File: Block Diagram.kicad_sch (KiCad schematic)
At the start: 0 parts

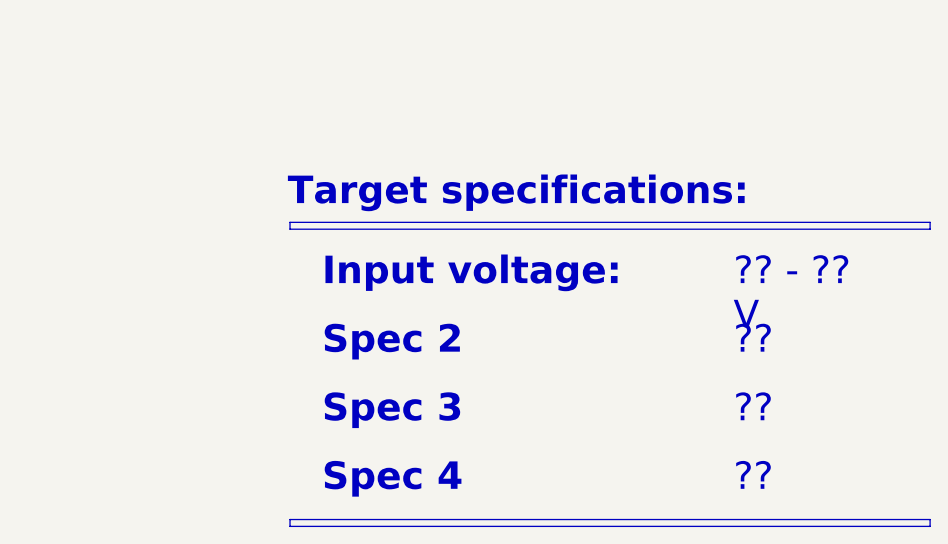
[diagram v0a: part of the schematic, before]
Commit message: Changed resistor position
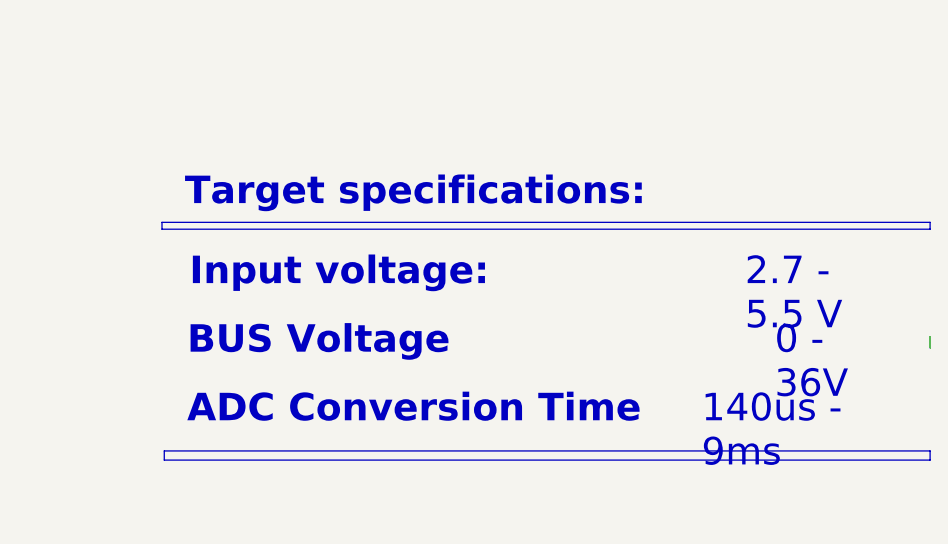
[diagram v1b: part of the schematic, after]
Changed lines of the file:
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@@
 	)
 	(rectangle
-		(start 331.47 237.49)
-		(end 402.59 238.252)
+		(start 317.5 229.87)
+		(end 402.59 230.886)
 		(stroke
 			(width 0)
@@
 	)
 	(rectangle
-		(start 331.47 204.47)
+		(start 317.246 204.47)
 		(end 402.59 205.232)
 		(stroke
@@
 		)
 	)
-	(text_box "Spec 3"
-		(exclude_from_sim no)
-		(at 332.74 220.98 0)
-		(size 41.91 7.62)
+	(text_box "ADC Conversion Time"
+		(exclude_from_sim no)
+		(at 317.754 220.98 0)
+		(size 56.896 7.62)
 		(margins 2.2859 2.2859 2.2859 2.2859)
 		(stroke
 			(width -0.0001)
-			(type default)
+			(type solid)
 		)
 		(fill
@@
 		)
 	)
-	(text_box "Spec 2"
-		(exclude_from_sim no)
-		(at 332.74 213.36 0)
+	(text_box "BUS Voltage"
+		(exclude_from_sim no)
+		(at 317.754 213.36 0)
 		(size 43.18 7.62)
 		(margins 2.2859 2.2859 2.2859 2.2859)
 		(stroke
 			(width -0.0001)
-			(type default)
+			(type solid)
 		)
 		(fill
@@
 	(text_box "Input voltage:"
 		(exclude_from_sim no)
-		(at 332.74 205.74 0)
+		(at 318.008 205.74 0)
 		(size 41.91 7.62)
 		(margins 2.2859 2.2859 2.2859 2.2859)
@@
 		)
 	)
-	(text_box "??"
-		(exclude_from_sim no)
-		(at 378.46 228.6 0)
+	(text_box "0 - 36V"
+		(exclude_from_sim no)
+		(at 383.032 213.36 0)
 		(size 24.13 7.62)
 		(margins 2.2859 2.2859 2.2859 2.2859)
 		(stroke
 			(width -0.0001)
-			(type default)
-		)
-		(fill
-			(type none)
-		)
-		(effects
-			(font
-				(face "Times New Roman")
-				(size 3.048 3.048)
-				(color 0 0 0 1)
-			)
-			(justify left top)
-		)
-	)
-	(text_box "??"
-		(exclude_from_sim no)
-		(at 378.46 213.36 0)
-		(size 24.13 7.62)
-		(margins 2.2859 2.2859 2.2859 2.2859)
-		(stroke
-			(width -0.0001)
-			(type default)
+			(type solid)
 		)
 		(fill
@@
 	(text_box "Target specifications:"
 		(exclude_from_sim no)
-		(at 328.93 196.85 0)
-		(size 73.66 7.62)
+		(at 317.5 196.85 0)
+		(size 85.09 7.62)
 		(margins 2.2859 2.2859 2.2859 2.2859)
 		(stroke
@@
 		)
 	)
-	(text_box "??"
-		(exclude_from_sim no)
-		(at 378.46 220.98 0)
-		(size 24.13 7.62)
+	(text_box "140us - 9ms"
+		(exclude_from_sim no)
+		(at 374.904 220.98 0)
+		(size 27.686 7.62)
 		(margins 2.2859 2.2859 2.2859 2.2859)
 		(stroke
 			(width -0.0001)
-			(type default)
+			(type solid)
 		)
 		(fill
@@
 		)
 	)
-	(text_box "?? - ?? V"
-		(exclude_from_sim no)
-		(at 378.46 205.74 0)
+	(text_box "2.7 - 5.5 V"
+		(exclude_from_sim no)
+		(at 379.73 205.74 0)
 		(size 24.13 7.62)
 		(margins 2.2859 2.2859 2.2859 2.2859)
 		(stroke
 			(width -0.0001)
-			(type default)
+			(type solid)
 		)
 		(fill
@@
 		)
 	)
-	(text_box "Spec 4"
-		(exclude_from_sim no)
-		(at 332.74 228.6 0)
-		(size 44.45 7.62)
-		(margins 2.2859 2.2859 2.2859 2.2859)
-		(stroke
-			(width -0.0001)
-			(type default)
-		)
-		(fill
-			(type none)
-		)
-		(effects
-			(font
-				(face "Times New Roman")
-				(size 3.048 3.048)
-				(thickness 0.4572)
-				(bold yes)
-				(color 0 0 0 1)
-			)
-			(justify left top)
-		)
-	)
 	(text_box "Block\nDescription"
 		(exclude_from_sim no)
@@
 		)
 	)
+	(wire
+		(pts
+			(xy 402.59 217.17) (xy 402.59 218.44)
+		)
+		(stroke
+			(width 0)
+			(type default)
+		)
+	)

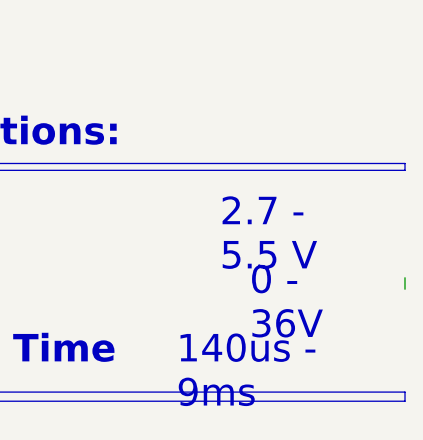
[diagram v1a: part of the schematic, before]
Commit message: Split I2C connector
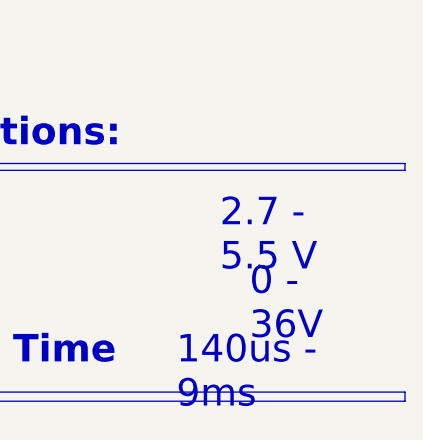
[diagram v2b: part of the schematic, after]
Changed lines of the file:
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@@
-		)
-	)
-	(wire
-		(pts
-			(xy 402.59 217.17) (xy 402.59 218.44)
-		)
-		(stroke
-			(width 0)
-			(type default)
 		)
 	)

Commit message: Outputs generated, ready for prototyping
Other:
- note added: "VCC"
- note removed: "+??V"
- note removed: "+A3V3"
